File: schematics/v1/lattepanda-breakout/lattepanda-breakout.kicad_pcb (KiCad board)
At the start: 2 copper layers, 31 x 58.4 mm, 6 parts, among them J1 RJ45, J2 PC-1818517, J3 PC-1818517, J4 Conn_02x04_Odd_Even, J5 Conn_02x15_Odd_Even, J6 Conn_02x02_Odd_Even

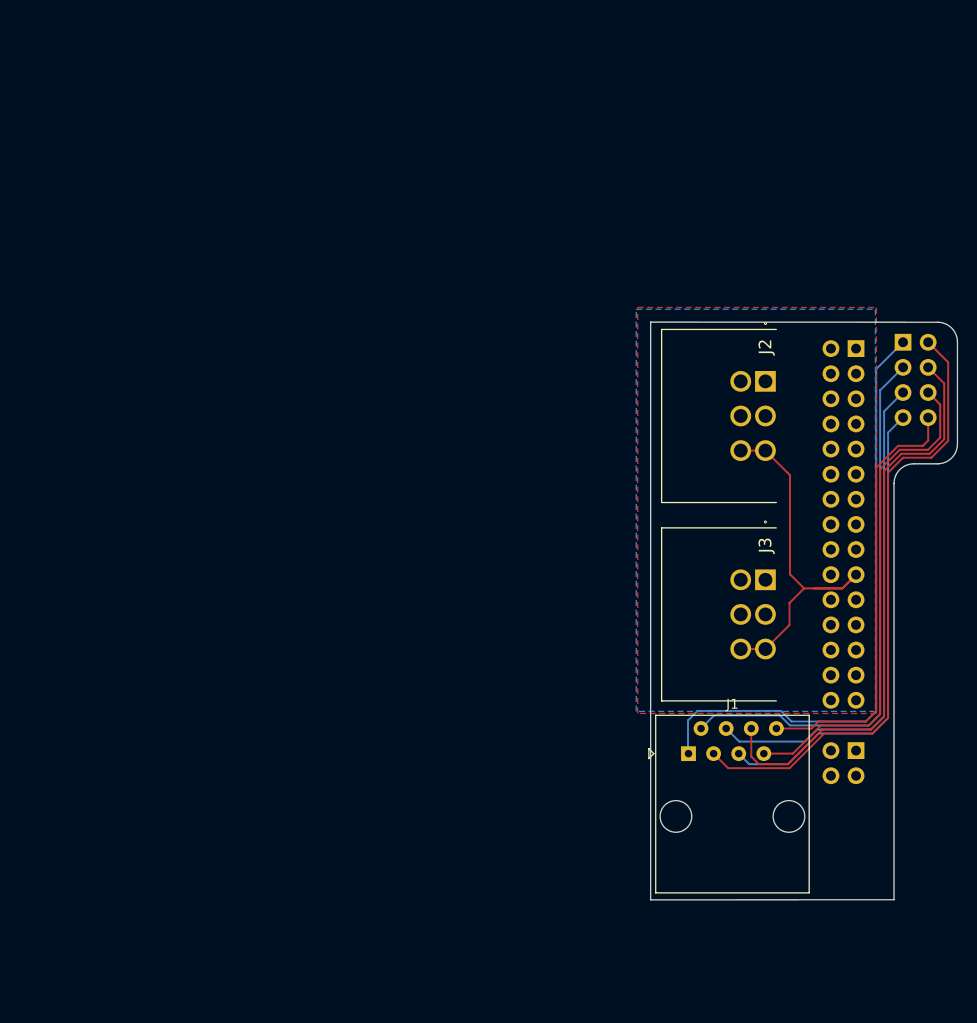
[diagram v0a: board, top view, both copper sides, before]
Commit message: update(lattepanda-breakout): rev2
added rs485 connection
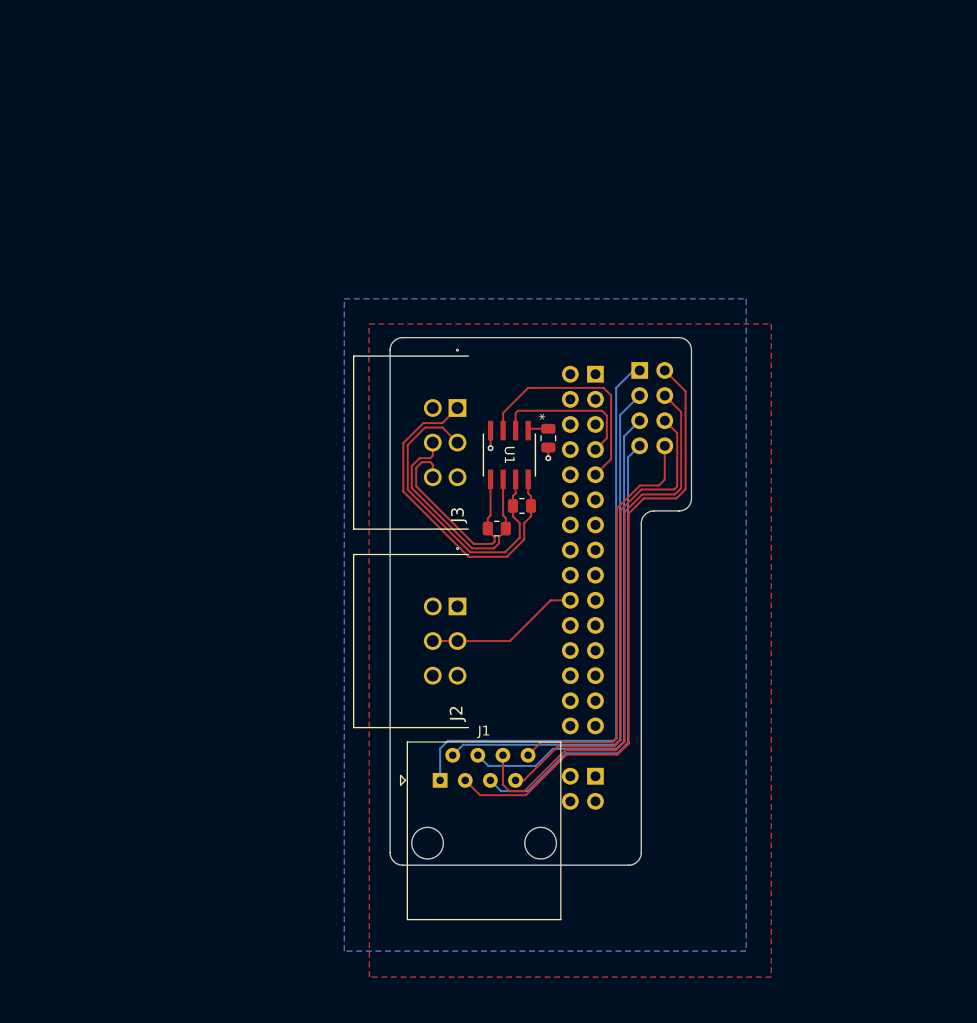
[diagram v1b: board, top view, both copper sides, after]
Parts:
- added C1: 0.1uF, Capacitor_SMD:C_0805_2012Metric, F.Cu at (71.9, 57.4)
- added R1: 120, Resistor_SMD:R_0805_2012Metric, F.Cu at (66.7, 66.5)
- added R2: 120, Resistor_SMD:R_0805_2012Metric, F.Cu at (69.2, 64.3)
- added U1: MAX22508, Link_Footprints:MAX22508, F.Cu at (67.9, 59.1)
- J2, J3: value PC-1818517 -> SDI12; footprint Link_Footprints:PC-1818517 -> Link_Footprints:PC-1053866
- moved J3 45.2 mm to (62.7, 54.4)
- moved J2 34.6 mm to (62.7, 74.4)
- moved J4 26.8 mm to (81.1, 50.6)
- moved J5 26.5 mm to (76.6, 50.9)
- moved J6 26.5 mm to (76.6, 91.6)
- moved J1 25.3 mm to (60.9, 92.0)
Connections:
- J2 pad 1: /SDI_PWR -> +5V
- J2 pad 2: /SDI_GND -> /SDI12
- J2 pad 3: /SDI_COMM -> GND
- J2 pad 4: /SDI_PWR -> +5V
- J2 pad 5: /SDI_GND -> /SDI12
- J2 pad 6: /SDI_COMM -> GND
- J3 pad 1: /SDI_PWR -> /RX+
- J3 pad 2: /SDI_GND -> /RX-
- J3 pad 3: /SDI_COMM -> GND
- J3 pad 4: /SDI_PWR -> +5V
- J3 pad 5: /SDI_GND -> /TX-
- J3 pad 6: /SDI_COMM -> /TX+
- J5 pad 19: /SDI_COMM -> unconnected-(J5-Pin_19-Pad19)
- J5 pad 20: unconnected-(J5-Pin_20-Pad20) -> /SDI12
- J5 pad 29: /SDI_PWR -> GND
- J5 pad 30: /SDI_GND -> +5V
- J5 pad 7: unconnected-(J5-Pin_7-Pad7) -> /RX
- J5 pad 9: unconnected-(J5-Pin_9-Pad9) -> /TX
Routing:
- net /SDI_COMM: track 39.0 -> 0.00 mm
- net /RX+: track 0.00 -> 34.0 mm
- net /RX-: track 0.00 -> 31.8 mm
- net /TX-: track 0.00 -> 24.8 mm
- net /TX: track 0.00 -> 22.7 mm
- net /TX+: track 0.00 -> 22.3 mm
- net /SDI12: track 0.00 -> 15.6 mm
- net /RX: track 0.00 -> 15.2 mm
- net GND: track 0.00 -> 2.86 mm, vias 0 -> 2
- net /LED_PWR_{-}: track 55.6 -> 53.2 mm
- net /LED_PWR_{+}: track 62.1 -> 60.0 mm
- net +5V: track 0.00 -> 2.11 mm
- net /BTN_PWR_{-}: track 51.1 -> 49.3 mm
- net /BTN_RST_{-}: track 44.1 -> 42.4 mm
- net /BTN_PWR_{+}: track 48.5 -> 46.9 mm
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- added copper zone on F.Cu, net +5V
- added copper zone on B.Cu, net GND
- removed copper zone on F.Cu, net /SDI_GND
- removed copper zone on B.Cu, net /SDI_PWR
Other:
- board size 31 x 58.4 mm -> 30.5 x 53.3 mm

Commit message: fix(breakout)
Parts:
- U1: value MAX22508 -> 21-0041_S8+2C_MXM
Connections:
- J5 pad 27: unconnected-(J5-Pin_27-Pad27) -> +5V
- J5 pad 28: unconnected-(J5-Pin_28-Pad28) -> GND
- J5 pad 29: GND -> +5V
- J5 pad 30: +5V -> GND
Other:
- board size 30.5 x 53.3 mm -> 30.5 x 54 mm
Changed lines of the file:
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@@
 		(sheetname "/")
 		(sheetfile "lattepanda-breakout.kicad_sch")
-		(units
-			(unit
-				(name "A")
-				(pins "8" "7" "6" "5" "4" "3" "2" "1")
-			)
-		)
 		(attr through_hole)
 		(duplicate_pad_numbers_are_jumpers no)
@@
 		)
 		(embedded_fonts no)
-		(model "${KICAD9_3DMODEL_DIR}/Connector_RJ.3dshapes/RJ45_Amphenol_54602-x08_Horizontal.wrl"
+		(model "${KIPRJMOD}/../libraries/models/54602-908LF.stp"
 			(offset
-				(xyz 0 0 0)
+				(xyz 4.5 3.75 10.5)
 			)
 			(scale
@@
 			)
 			(rotate
-				(xyz 0 0 0)
+				(xyz -90 -0 -90)
 			)
 		)
@@
 			)
 		)
-		(property "Value" "MAX22508"
+		(property "Value" "21-0041_S8+2C_MXM"
 			(at 0 0 270)
 			(unlocked yes)
@@
 		(sheetname "/")
 		(sheetfile "lattepanda-breakout.kicad_sch")
-		(units
-			(unit
-				(name "A")
-				(pins "1" "2" "3" "4" "8" "7" "6" "5")
-			)
-		)
 		(attr smd)
 		(duplicate_pad_numbers_are_jumpers no)
@@
 			)
 		)
+		(fp_text user "*"
+			(at -2.7178 -3.5814 270)
+			(layer "F.SilkS")
+			(effects
+				(font
+					(size 1 1)
+					(thickness 0.15)
+				)
+			)
+		)
 		(fp_text user "${REFERENCE}"
 			(at 0 0 270)
@@
 		)
 		(embedded_fonts no)
+		(model "${KIPRJMOD}/../libraries/models/MAX22508.step"
+			(offset
+				(xyz 0 0 0)
+			)
+			(scale
+				(xyz 1 1 1)
+			)
+			(rotate
+				(xyz 0 0 0)
+			)
+		)
 	)
 	(footprint "Link_Footprints:PC-1053866"
@@
 			(layers "*.Cu" "*.Mask")
 			(remove_unused_layers no)
-			(net "unconnected-(J5-Pin_27-Pad27)")
+			(net "+5V")
 			(pinfunction "Pin_27_27")
-			(pintype "passive+no_connect")
+			(pintype "passive")
 		)
 		(pad "28" thru_hole circle
@@
 			(layers "*.Cu" "*.Mask")
 			(remove_unused_layers no)
-			(net "unconnected-(J5-Pin_28-Pad28)")
+			(net "GND")
 			(pinfunction "Pin_28_28")
-			(pintype "passive+no_connect")
+			(pintype "passive")
 		)
 		(pad "29" thru_hole circle
@@
 			(layers "*.Cu" "*.Mask")
 			(remove_unused_layers no)
-			(net "GND")
+			(net "+5V")
 			(pinfunction "Pin_29_29")
 			(pintype "passive")
@@
 			(layers "*.Cu" "*.Mask")
 			(remove_unused_layers no)
-			(net "+5V")
+			(net "GND")
 			(pinfunction "Pin_30_30")
 			(pintype "passive")
@@
 	(gr_line
 		(start 55.88 48.514)
-		(end 55.88 99.314)
+		(end 55.88 99.939974)
 		(stroke
 			(width 0.05)
@@
 	)
 	(gr_arc
-		(start 57.15 100.584)
-		(mid 56.251974 100.212026)
-		(end 55.88 99.314)
+		(start 57.15 101.209974)
+		(mid 56.251974 100.838)
+		(end 55.88 99.939974)
 		(stroke
 			(width 0.05)
@@
 	)
 	(gr_line
-		(start 57.15 100.584)
-		(end 80.01 100.584)
+		(start 57.15 101.219)
+		(end 80.01 101.219)
 		(stroke
 			(width 0.05)
@@
 	)
 	(gr_arc
-		(start 81.28 99.314)
-		(mid 80.908026 100.212026)
-		(end 80.01 100.584)
+		(start 81.28 99.939974)
+		(mid 80.908026 100.838)
+		(end 80.01 101.209974)
 		(stroke
 			(width 0.05)
@@
 	)
 	(gr_line
-		(start 81.28 99.314)
+		(start 81.28 99.939974)
 		(end 81.28 66.04)
 		(stroke
@@
 	(dimension
 		(type orthogonal)
+		(layer "Edge.Cuts")
+		(pts
+			(xy 81.28 66.04) (xy 86.36 63.5)
+		)
+		(height 3.556)
+		(orientation 0)
+		(format
+			(prefix "")
+			(suffix "")
+			(units 3)
+			(units_format 0)
+			(precision 4)
+			(suppress_zeroes yes)
+		)
+		(style
+			(thickness 0.05)
+			(arrow_length 1.27)
+			(text_position_mode 0)
+			(arrow_direction outward)
+			(extension_height 0.58642)
+			(extension_offset 0.5)
+			(keep_text_aligned yes)
+		)
+		(gr_text "200"
+			(at 83.82 68.446 0)
+			(layer "Edge.Cuts")
+			(effects
+				(font
+					(size 1 1)
+					(thickness 0.15)
+				)
+			)
+		)
+	)
+	(dimension
+		(type orthogonal)
 		(layer "User.1")
 		(pts
 			(xy 85.09 47.244) (xy 80.01 100.584)
 		)
-		(height 23.246)
+		(height 7.366)
 		(orientation 1)
 		(format
@@
 		)
 		(gr_text "2100"
-			(at 107.186 73.914 90)
+			(at 91.306 73.914 90)
 			(layer "User.1")
 			(effects
@@
 			(xy 76.649084 50.941257) (xy 76.649084 91.581257)
 		)
-		(height 20.828)
+		(height 11.742916)
 		(orientation 1)
 		(format
@@
 			(thickness 0.05)
 			(arrow_length 1.27)
-			(text_position_mode 0)
+			(text_position_mode 2)
 			(arrow_direction outward)
 			(extension_height 0.58642)
@@
 		)
 		(gr_text "1600"
-			(at 96.327084 71.261257 90)
+			(at 88.392 71.12 90)
 			(layer "User.1")
 			(effects
@@
 			(xy 76.649084 50.941257) (xy 81.119484 50.560257)
 		)
-		(height 20.828)
+		(height 11.742916)
 		(orientation 1)
 		(format
@@
 		)
 		(gr_text "15"
-			(at 99.001084 50.750757 90)
+			(at 89.916 50.750757 90)
 			(layer "User.1")
 			(effects
@@
 		(polygon
 			(pts
-				(xy 53.745502 45.861257) (xy 94.429084 45.861257) (xy 94.429084 111.901257) (xy 53.788917 111.901257)
+				(xy 47.594775 32.893) (xy 98.933 32.893) (xy 98.933 111.901257) (xy 47.646717 111.901257)
 			)
 		)
@@
 		(polygon
 			(pts
-				(xy 51.249084 43.321257) (xy 91.889084 43.321257) (xy 91.889084 109.273657) (xy 51.249084 109.273657)
+				(xy 42.545 31.877) (xy 96.901 31.877) (xy 96.901 109.273657) (xy 42.545 109.273657)
 			)
 		)

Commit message: update(lattepanda-breakout)
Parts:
- removed the J6 at (76.6, 91.6)
- added C2: 0.1uF, Capacitor_SMD:C_0805_2012Metric, F.Cu at (19.9, 49.8)
- added C3: 0.1uF, Capacitor_SMD:C_0805_2012Metric, F.Cu at (19.9, 52.8)
- added C4: 0.1uF, Capacitor_SMD:C_0805_2012Metric, F.Cu at (19.9, 55.8)
- added C5: 0.1uF, Capacitor_SMD:C_0805_2012Metric, F.Cu at (19.9, 58.8)
- added C6: 0.1uF, Capacitor_SMD:C_0805_2012Metric, F.Cu at (19.9, 61.8)
- added C7: 1uF, Capacitor_SMD:C_0805_2012Metric, F.Cu at (19.9, 64.8)
- added C8: 1uF, Capacitor_SMD:C_0805_2012Metric, F.Cu at (19.9, 67.8)
- added J1: Arduino, Connector_PinHeader_2.54mm:PinHeader_2x05_P2.54mm_Vertical, B.Cu at (76.8, 50.9)
- added J3: COM(RS232/485), Connector_PinSocket_2.54mm:PinSocket_2x05_P2.54mm_Vertical, B.Cu at (81.3, 34.7)
- added J7: RS232, Link_Footprints:PC-1053866, F.Cu at (79.4, 95.0)
- added U2: TRSF3232ECD, Link_Footprints:TRFS3232E, F.Cu at (32.3, 69.7)
- added U3: TLV75533PDBV, Package_TO_SOT_SMD:SOT-23-5, F.Cu at (40.9, 66.7)
- J2: renamed from J5; value Conn_02x15_Odd_Even -> Arduino; footprint Connector_PinHeader_2.54mm:PinHeader_2x15_P2.54mm_Vertical -> Connector_PinHeader_2.54mm:PinHeader_2x06_P2.54mm_Vertical_SMD
- J4: value Conn_02x04_Odd_Even -> Front Panel; footprint Connector_PinSocket_2.54mm:PinSocket_2x04_P2.54mm_Vertical -> Connector_PinSocket_2.54mm:PinSocket_2x05_P2.54mm_Vertical
- J6: renamed from J3; value SDI12 -> RS485
- J8: renamed from J1; value RJ45 -> PiKVM
- U1: value 21-0041_S8+2C_MXM -> MAX22508
- moved J2 29.2 mm to (75.6, 80.1)
- moved J8 1.14 mm to (59.8, 92.0)
- moved J4 0.16 mm to (81.3, 50.5)
- renumbered J2 to J5
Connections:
- J2 pad 10: unconnected-(J5-Pin_10-Pad10) -> GND
- J2 pad 11: unconnected-(J5-Pin_11-Pad11) -> +5V
- J2 pad 12: unconnected-(J5-Pin_12-Pad12) -> GND
- J2 pad 2: unconnected-(J5-Pin_2-Pad2) -> /SDI12
- J2 pad 7: /RX -> unconnected-(J2-Pin_7-Pad7)
- J2 pad 9: /TX -> +5V
- R1 pad 1: /TX- -> /RX-
- R1 pad 2: /TX+ -> /RX+
- R2 pad 1: /RX- -> /TX-
- R2 pad 2: /RX+ -> /TX+
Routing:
- net /LED_HDD_{+}: track 62.5 -> 0.00 mm
- net /LED_PWR_{+}: track 60.0 -> 0.00 mm
- net /LED_HDD_{-}: track 57.6 -> 0.00 mm
- net /LED_PWR_{-}: track 53.2 -> 0.00 mm
- net /BTN_RST_{+}: track 49.4 -> 0.00 mm
- net /BTN_PWR_{-}: track 49.3 -> 0.00 mm
- net /BTN_PWR_{+}: track 46.9 -> 0.00 mm
- net /BTN_RST_{-}: track 42.4 -> 0.00 mm
- net /RX+: track 34.0 -> 0.00 mm
- net /RX-: track 31.8 -> 0.00 mm
- net /TX-: track 24.8 -> 0.00 mm
- net /TX: track 22.7 -> 0.00 mm
- net /TX+: track 22.3 -> 0.00 mm
- net /SDI12: track 15.6 -> 0.00 mm
- net /RX: track 15.2 -> 0.00 mm
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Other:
- board size 30.5 x 54 mm -> 35.6 x 69.8 mm

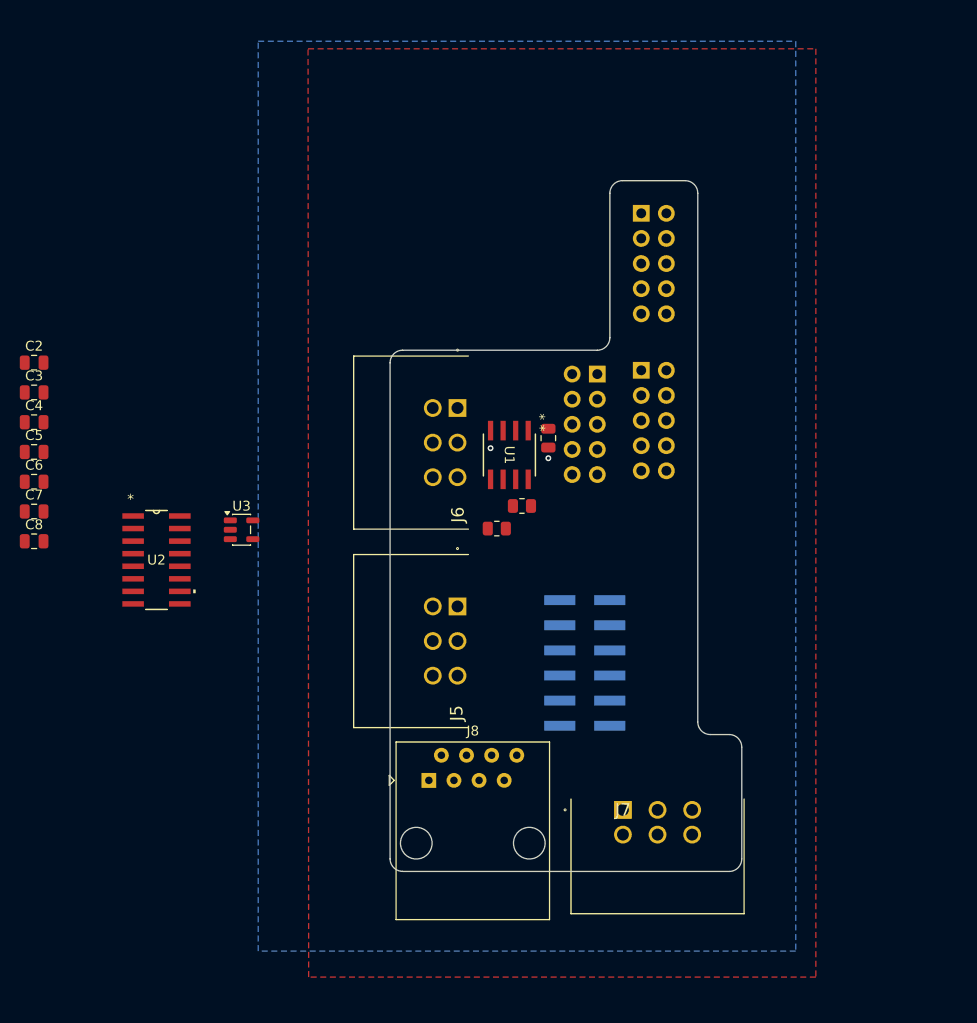
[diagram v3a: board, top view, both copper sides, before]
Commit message: update(lattepanda-breakout): still need to To make routing a little bit easier, could switch to 4 layer 1. Finish routing for RS232 2. Add differentials for RS422 to tsd 3. Consider switching connectors? 4. Verify wiring of Rj45 connector (changed from original breakout)
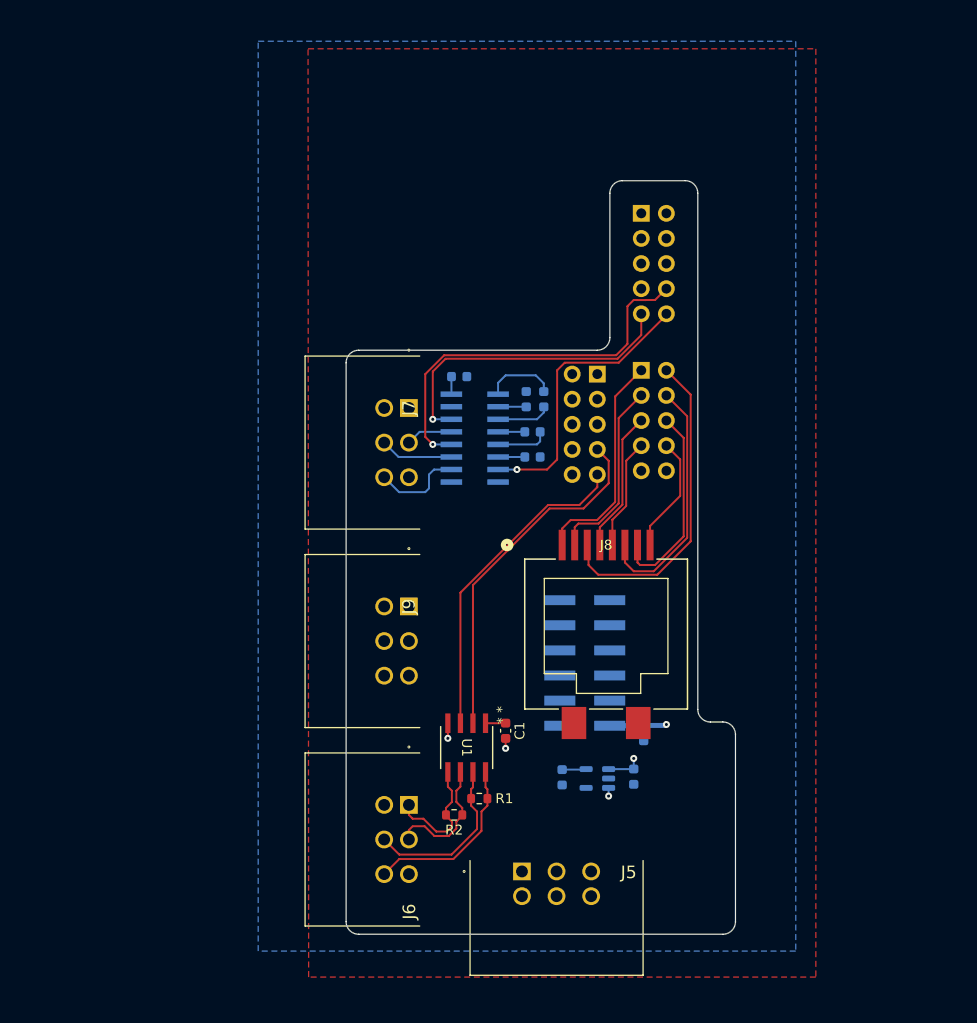
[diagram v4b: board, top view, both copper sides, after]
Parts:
- added C9: 1uF, Capacitor_SMD:C_0603_1608Metric, B.Cu at (81.5, 87.2)
- added J9: RS422, Link_Footprints:PC-1053866, F.Cu at (57.8, 74.4)
- C1: footprint Capacitor_SMD:C_0805_2012Metric -> Capacitor_SMD:C_0603_1608Metric
- C2, C3, C4, C5, C6, C7, C8: footprint Capacitor_SMD:C_0805_2012Metric -> Capacitor_SMD:C_0603_1608Metric; moved to B.Cu
- J8: footprint Connector_RJ:RJ45_Amphenol_54602-x08_Horizontal -> Link_Footprints:rj45_smd
- R1, R2: footprint Resistor_SMD:R_0805_2012Metric -> Resistor_SMD:R_0603_1608Metric
- U2, U3: moved to B.Cu
- moved C7 66.3 mm to (80.5, 91.6), turned to -90 degrees
- moved C8 58.5 mm to (73.3, 91.7), turned to -90 degrees
- moved C2 51.7 mm to (71.4, 53.5), turned to -90 degrees
- moved C3 50.6 mm to (70.3, 56.8)
- moved C4 50.5 mm to (70.3, 59.3), turned to 180 degrees
- moved C5 50.0 mm to (69.6, 53.5), turned to 90 degrees
- moved J7 46.0 mm to (57.8, 54.4), turned to -90 degrees
- moved C6 44.3 mm to (62.9, 51.2)
- moved U3 43.9 mm to (76.8, 91.8), turned to 180 degrees
- moved J6 40.4 mm to (57.8, 94.5)
- moved U2 34.5 mm to (64.4, 57.4), turned to 180 degrees
- moved R2 32.0 mm to (62.4, 95.5), turned to 180 degrees
- moved C1 29.9 mm to (67.6, 87.0)
- moved U1 29.9 mm to (63.6, 88.7)
- moved J5 27.6 mm to (69.2, 101.2), turned to 0 degrees
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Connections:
- net /RX renamed /485_RX
- net /TX renamed /485_TX
- J6 pad 1: /RX+ -> /485_TX+
- J6 pad 2: /RX- -> /485_TX-
- J6 pad 5: /TX- -> /485_RX-
- J6 pad 6: /TX+ -> /485_RX+
- R1 pad 1: /RX- -> /485_RX-
- R1 pad 2: /RX+ -> /485_RX+
- R2 pad 1: /TX- -> /485_TX-
- R2 pad 2: /TX+ -> /485_TX+
- U1 pad 5: /TX+ -> /485_TX+
- U1 pad 6: /TX- -> /485_TX-
- U1 pad 7: /RX- -> /485_RX-
- U1 pad 8: /RX+ -> /485_RX+
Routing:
- net /LP_TX: track 0.00 -> 39.5 mm, vias 0 -> 1
- net /485_RX: track 0.00 -> 35.9 mm
- net /485_TX: track 0.00 -> 32.7 mm
- net /LED_HDD_{+}: track 0.00 -> 32.5 mm
- net /LP_RX: track 0.00 -> 31.5 mm, vias 0 -> 1
- net /LP_DCD: track 0.00 -> 28.9 mm, vias 0 -> 1
- net /LED_HDD_{-}: track 0.00 -> 25.1 mm
- net /LED_PWR_{+}: track 0.00 -> 22.5 mm
- net /BTN_RST_{+}: track 0.00 -> 20.2 mm
- net /LED_PWR_{-}: track 0.00 -> 19.1 mm
- net /485_RX+: track 0.00 -> 17.9 mm
- net /485_RX-: track 0.00 -> 17.2 mm
- net /BTN_PWR_{-}: track 0.00 -> 14.3 mm
- net /485_TX-: track 0.00 -> 13.0 mm
- net /485_TX+: track 0.00 -> 12.5 mm
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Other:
- board size 35.6 x 69.8 mm -> 39.4 x 76.2 mm
- copper layers 2 -> 4
